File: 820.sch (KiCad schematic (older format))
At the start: 125 parts, among them J1 PJ301BM, J10 PJ301BM, J2 PJ301BM, J4 PJ301BM, J5 PJ301BM, J6 PJ301BM, J7 PJ301BM, J8 PJ301BM, J9 PJ301BM, P1 CONN_02X05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

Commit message: updates for final prototype, changed matched pair back to SOT-363
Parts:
- R16: value 91K -> 82K
- R17: value 56K -> 27K
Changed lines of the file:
@@
 P 10525 7575
 F 0 "R17" V 10605 7575 50  0000 C CNN
-F 1 "56K" V 10425 7575 50  0000 C CNN
+F 1 "27K" V 10425 7575 50  0000 C CNN
 F 2 "MyModules:SM0603-R-JRL" H 10525 7575 60  0001 C CNN
 F 3 "" H 10525 7575 60  0001 C CNN
@@
 P 8775 6950
 F 0 "R16" V 8855 6950 50  0000 C CNN
-F 1 "91K" V 8675 6950 50  0000 C CNN
+F 1 "82K" V 8675 6950 50  0000 C CNN
 F 2 "MyModules:SM0603-R-JRL" H 8775 6950 60  0001 C CNN
 F 3 "" H 8775 6950 60  0001 C CNN

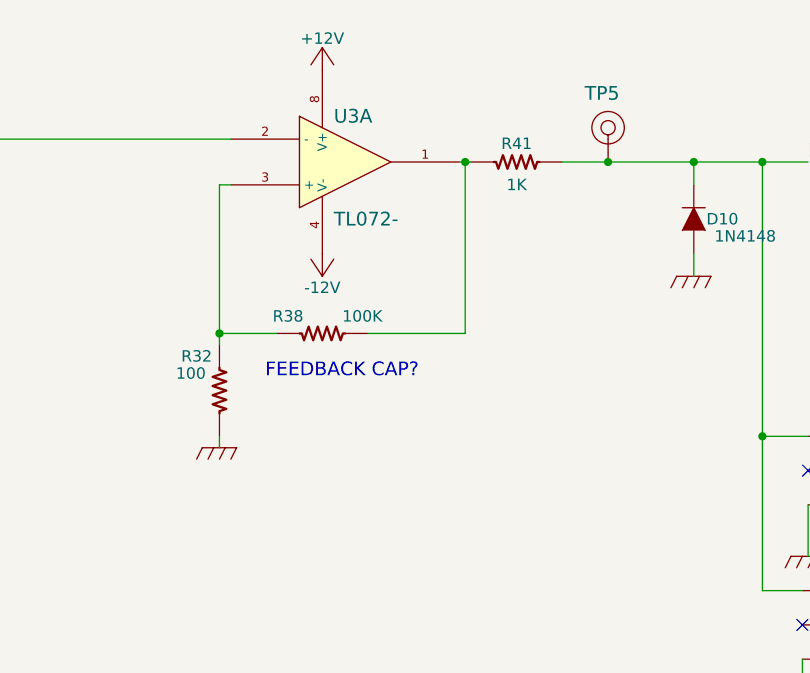
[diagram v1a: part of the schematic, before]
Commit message: final prototype ordred, built and tested, committing now and then branching to panelization
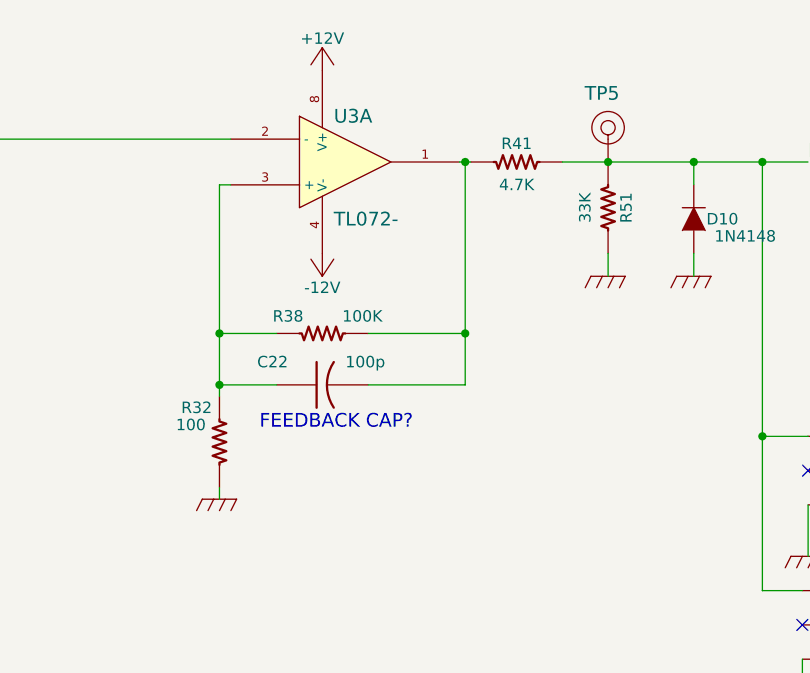
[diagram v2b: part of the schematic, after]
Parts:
- added C22: 100p, MyModules:SM0603-C-JRL, symbol C_US
- added R51: 33K, MyModules:SM0603-R-JRL, symbol R_US
- R41: value 1K -> 4.7K
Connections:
- net GND: now also R51.2
- net PULSE: now also R51.1
- net at R38.2, R41.1, U3.1: now also C22.2
- net at R32.1, R38.1, U3.3 (+): now also C22.1
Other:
- moved on the sheet: R32
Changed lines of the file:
@@
 $EndComp
 $Comp
-L GND_R #PWR70
+L GND_R #PWR71
 U 1 1 5B4130A7
 P 17575 8500
-F 0 "#PWR70" H 17575 8500 30  0001 C CNN
+F 0 "#PWR71" H 17575 8500 30  0001 C CNN
 F 1 "GND_R" H 17575 8400 30  0001 C CNN
 F 2 "" H 17575 8500 60  0000 C CNN
@@
 $EndComp
 $Comp
-L +12V #PWR69
+L +12V #PWR70
 U 1 1 5B4130C5
 P 17575 6350
-F 0 "#PWR69" H 17575 6200 50  0001 C CNN
+F 0 "#PWR70" H 17575 6200 50  0001 C CNN
 F 1 "+12V" H 17575 6490 50  0000 C CNN
 F 2 "" H 17575 6350 60  0000 C CNN
@@
 P 16950 12325
 F 0 "R41" V 17030 12325 50  0000 C CNN
-F 1 "1K" V 16850 12325 50  0000 C CNN
+F 1 "4.7K" V 16850 12325 50  0000 C CNN
 F 2 "MyModules:SM0603-R-JRL" H 16950 12325 60  0001 C CNN
 F 3 "" H 16950 12325 60  0001 C CNN
@@
 $EndComp
 $Comp
-L -12V #PWR73
+L -12V #PWR74
 U 1 1 5B41314E
 P 18075 8225
-F 0 "#PWR73" H 18075 8325 30  0001 C CNN
+F 0 "#PWR74" H 18075 8325 30  0001 C CNN
 F 1 "-12V" H 18075 8375 50  0000 C CNN
 F 2 "~" H 18075 8225 60  0000 C CNN
@@
 $EndComp
 $Comp
-L +12V #PWR72
+L +12V #PWR73
 U 1 1 5B413154
 P 18075 7425
-F 0 "#PWR72" H 18075 7275 50  0001 C CNN
+F 0 "#PWR73" H 18075 7275 50  0001 C CNN
 F 1 "+12V" H 18075 7565 50  0000 C CNN
 F 2 "" H 18075 7425 60  0000 C CNN
@@
 $EndComp
 $Comp
-L GND_R #PWR74
+L GND_R #PWR75
 U 1 1 5B413252
 P 18100 10875
-F 0 "#PWR74" H 18100 10875 30  0001 C CNN
+F 0 "#PWR75" H 18100 10875 30  0001 C CNN
 F 1 "GND_R" H 18100 10775 30  0001 C CNN
 F 2 "" H 18100 10875 60  0000 C CNN
@@
 L R_US R32
 U 1 1 5B41350D
-P 15650 13325
-F 0 "R32" H 15750 13475 50  0000 C CNN
-F 1 "100" H 15775 13400 50  0000 C CNN
-F 2 "MyModules:SM0603-R-JRL" H 15650 13325 60  0001 C CNN
-F 3 "" H 15650 13325 60  0001 C CNN
-F 4 "P10.0KCCT-ND" V 15650 13325 60  0001 C CNN "Digikey"
-	1    15650 13325
+P 15650 13550
+F 0 "R32" H 15750 13700 50  0000 C CNN
+F 1 "100" H 15775 13625 50  0000 C CNN
+F 2 "MyModules:SM0603-R-JRL" H 15650 13550 60  0001 C CNN
+F 3 "" H 15650 13550 60  0001 C CNN
+F 4 "P10.0KCCT-ND" V 15650 13550 60  0001 C CNN "Digikey"
+	1    15650 13550
 	-1   0    0    -1
 $EndComp
 $Comp
-L GND_R #PWR71
+L GND_R #PWR72
 U 1 1 5B41351B
 P 17725 12825
-F 0 "#PWR71" H 17725 12825 30  0001 C CNN
+F 0 "#PWR72" H 17725 12825 30  0001 C CNN
 F 1 "GND_R" H 17725 12725 30  0001 C CNN
 F 2 "" H 17725 12825 60  0000 C CNN
@@
 L GND_R #PWR58
 U 1 1 5B413522
-P 15650 13575
-F 0 "#PWR58" H 15650 13575 30  0001 C CNN
-F 1 "GND_R" H 15650 13475 30  0001 C CNN
-F 2 "" H 15650 13575 60  0000 C CNN
-F 3 "" H 15650 13575 60  0000 C CNN
-	1    15650 13575
+P 15650 13800
+F 0 "#PWR58" H 15650 13800 30  0001 C CNN
+F 1 "GND_R" H 15650 13700 30  0001 C CNN
+F 2 "" H 15650 13800 60  0000 C CNN
+F 3 "" H 15650 13800 60  0000 C CNN
+	1    15650 13800
 	1    0    0    -1
 $EndComp
@@
 	15700 12425 15650 12425
 Wire Wire Line
-	15650 12425 15650 13125
+	15650 12425 15650 13350
 Wire Wire Line
 	16300 13075 16725 13075
 Wire Wire Line
-	16725 13075 16725 12325
+	16725 12325 16725 13300
 Connection ~ 16725 12325
 Wire Wire Line
@@
 Connection ~ 15650 13075
 Wire Wire Line
-	15650 13525 15650 13575
+	15650 13750 15650 13800
 Wire Wire Line
 	13925 8375 14425 8375
@@
 	18025 14200 18200 14200
 $Comp
-L GND_R #PWR75
+L GND_R #PWR76
 U 1 1 5B4223A3
 P 18200 14700
-F 0 "#PWR75" H 18200 14700 30  0001 C CNN
+F 0 "#PWR76" H 18200 14700 30  0001 C CNN
 F 1 "GND_R" H 18200 14600 30  0001 C CNN
 F 2 "" H 18200 14700 60  0000 C CNN
@@
 	18200 14700 18200 14500
 $Comp
-L GND_R #PWR76
+L GND_R #PWR77
 U 1 1 5B422AC8
 P 18225 14050
-F 0 "#PWR76" H 18225 14050 30  0001 C CNN
+F 0 "#PWR77" H 18225 14050 30  0001 C CNN
 F 1 "GND_R" H 18225 13950 30  0001 C CNN
 F 2 "" H 18225 14050 60  0000 C CNN
@@
 	18225 14050 18225 13825
 $Comp
-L GND_R #PWR78
+L GND_R #PWR79
 U 1 1 5B423676
 P 19875 11075
-F 0 "#PWR78" H 19875 11075 30  0001 C CNN
+F 0 "#PWR79" H 19875 11075 30  0001 C CNN
 F 1 "GND_R" H 19875 10975 30  0001 C CNN
 F 2 "" H 19875 11075 60  0000 C CNN
@@
 NoConn ~ 19900 12075
 $Comp
-L GND_R #PWR79
+L GND_R #PWR80
 U 1 1 5B42596F
 P 19900 12400
-F 0 "#PWR79" H 19900 12400 30  0001 C CNN
+F 0 "#PWR80" H 19900 12400 30  0001 C CNN
 F 1 "GND_R" H 19900 12300 30  0001 C CNN
 F 2 "" H 19900 12400 60  0000 C CNN
@@
 Connection ~ 14400 11600
 $Comp
-L GND_R #PWR77
+L GND_R #PWR78
 U 1 1 5B4277DE
 P 19475 8600
-F 0 "#PWR77" H 19475 8600 30  0001 C CNN
+F 0 "#PWR78" H 19475 8600 30  0001 C CNN
 F 1 "GND_R" H 19475 8500 30  0001 C CNN
 F 2 "" H 19475 8600 60  0000 C CNN
@@
 	3025 2500 3025 2000
 Connection ~ 2875 2500
-Text Notes 15850 13275 0    60   ~ 0
+Text Notes 15825 13500 0    60   ~ 0
 FEEDBACK CAP?
 $Comp
@@
 Wire Wire Line
 	10925 8125 10925 8075
+$Comp
+L C_US C22
+U 1 1 5CB038BB
+P 16100 13300
+F 0 "C22" V 16200 13450 50  0000 L CNN
+F 1 "100p" V 16200 13025 50  0000 L CNN
+F 2 "MyModules:SM0603-C-JRL" H 16100 13300 60  0001 C CNN
+F 3 "" H 16100 13300 60  0000 C CNN
+F 4 "X7R" V 16375 13425 50  0001 C CNN "Type"
+	1    16100 13300
+	0    -1   -1   0
+$EndComp
+Wire Wire Line
+	15900 13300 15650 13300
+Connection ~ 15650 13300
+Wire Wire Line
+	16725 13300 16300 13300
+Connection ~ 16725 13075
+$Comp
+L R_US R51
+U 1 1 5CB06BAA
+P 17350 12525
+F 0 "R51" V 17430 12525 50  0000 C CNN
+F 1 "33K" V 17250 12525 50  0000 C CNN
+F 2 "MyModules:SM0603-R-JRL" H 17350 12525 60  0001 C CNN
+F 3 "" H 17350 12525 60  0001 C CNN
+F 4 "P10.0KCCT-ND" V 17350 12525 60  0001 C CNN "Digikey"
+	1    17350 12525
+	1    0    0    -1
+$EndComp
+$Comp
+L GND_R #PWR69
+U 1 1 5CB06D5B
+P 17350 12825
+F 0 "#PWR69" H 17350 12825 30  0001 C CNN
+F 1 "GND_R" H 17350 12725 30  0001 C CNN
+F 2 "" H 17350 12825 60  0000 C CNN
+F 3 "" H 17350 12825 60  0000 C CNN
+	1    17350 12825
+	1    0    0    -1
+$EndComp
+Wire Wire Line
+	17350 12725 17350 12825
 $EndSCHEMATC
